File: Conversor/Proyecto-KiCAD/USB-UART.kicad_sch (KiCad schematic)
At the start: 30 parts, among them P11 USB-B, Q5 IRF7425, SW5 Switch, U14 FT232BL, U15 LP2985-3.3, Y1 6 MHz

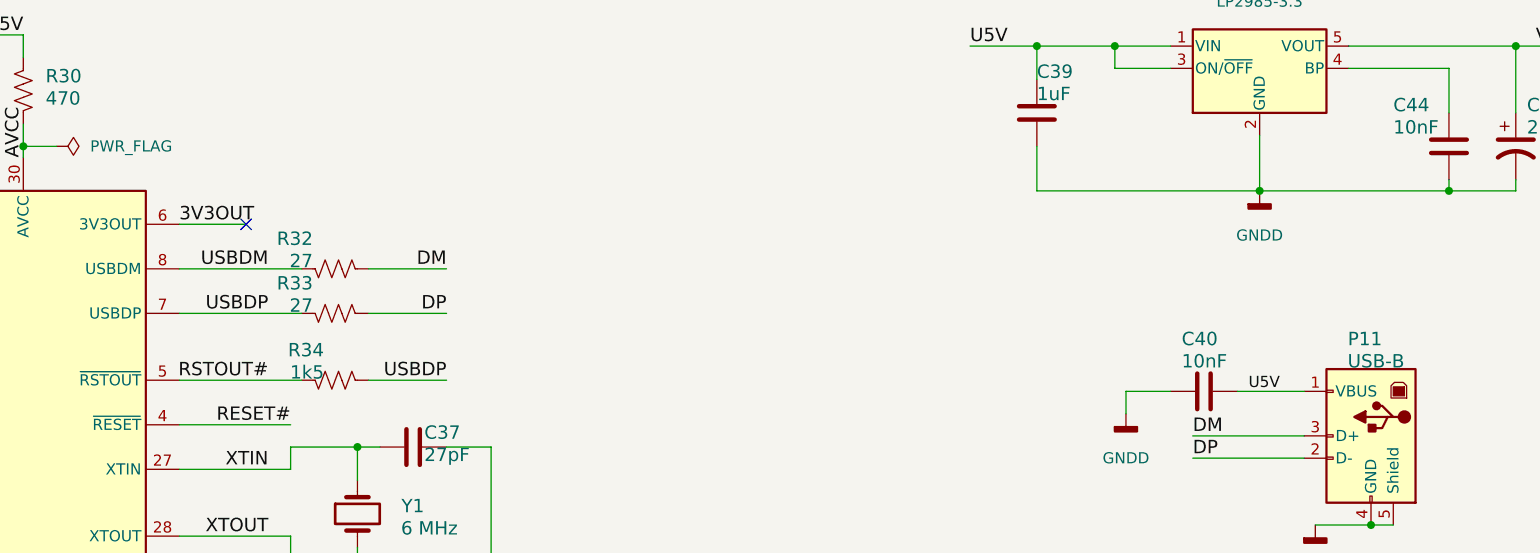
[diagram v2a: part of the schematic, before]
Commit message: Comenzar a asignar footprints a todos los componentes
- Agregado un header para conectar el módulo de tarjeta SD de Arduino
por SPI
- Los GNDs conectados por resistencias nulas son para conectar los GNDs
en caso de que fuera necesario
- Agregar una nota de aplicaión de aislación para I2C (creo que como
estan conectados SDAO y SDAI está bien)
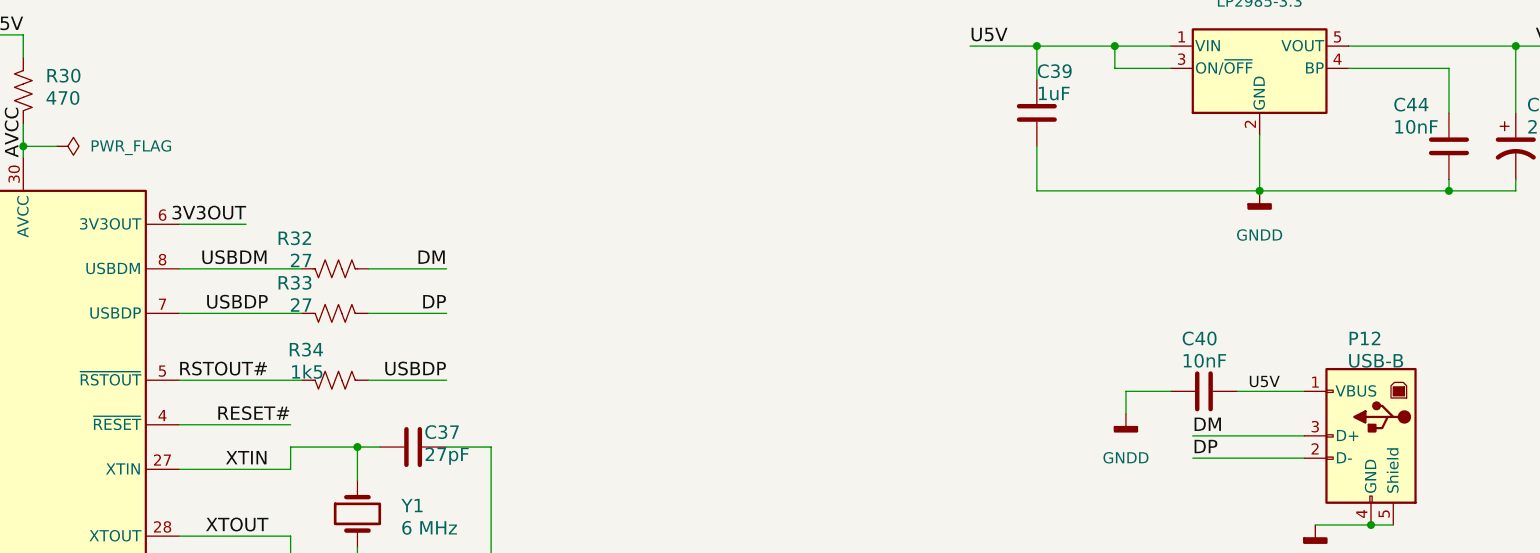
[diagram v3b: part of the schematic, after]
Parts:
- C34, C35, C36, C37, C38, C40, C41, C42, C44, C45, C47: footprint (none) -> Capacitor_SMD:C_1206_3216Metric_Pad1.33x1.80mm_HandSolder
- LED5, LED6: footprint (none) -> Diode_SMD:D_1206_3216Metric_Pad1.42x1.75mm_HandSolder
- P12: renamed from P11; footprint (none) -> Connector_USB:USB_B_Lumberg_2411_02_Horizontal
- R29, R30, R31, R32, R33, R34, R35, R36: footprint (none) -> Resistor_SMD:R_1206_3216Metric_Pad1.30x1.75mm_HandSolder
- Y1: footprint (none) -> Crystal:Crystal_HC18-U_Vertical
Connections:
- no-connect marks 12 -> 11
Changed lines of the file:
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@@
   (no_connect (at 96.52 107.95))
   (no_connect (at 50.8 67.31))
-  (no_connect (at 104.14 62.23))
   (no_connect (at 50.8 72.39))
   (no_connect (at 50.8 69.85))
@@
     (effects (font (size 1.524 1.524)) (justify right bottom))
   )
-  (label "3V3OUT" (at 96.52 62.23 0)
-    (effects (font (size 1.524 1.524)) (justify left bottom))
+  (label "3V3OUT" (at 104.14 62.23 180)
+    (effects (font (size 1.524 1.524)) (justify right bottom))
   )
   (label "U5V" (at 57.15 189.23 90)
@@
       (effects (font (size 1.524 1.524)) (justify right top))
     )
-    (property "Footprint" "" (id 2) (at 127 88.5952 0)
+    (property "Footprint" "Capacitor_SMD:C_1206_3216Metric_Pad1.33x1.80mm_HandSolder" (id 2) (at 127 88.5952 0)
       (effects (font (size 1.27 1.27)) hide)
     )
@@
       (effects (font (size 1.524 1.524)) (justify right top))
     )
-    (property "Footprint" "" (id 2) (at 114.046 66.294 90)
+    (property "Footprint" "Resistor_SMD:R_1206_3216Metric_Pad1.30x1.75mm_HandSolder" (id 2) (at 114.046 66.294 90)
       (effects (font (size 1.27 1.27)) hide)
     )
@@
       (effects (font (size 1.524 1.524)) (justify left bottom))
     )
-    (property "Footprint" "" (id 2) (at 187.96 132.08 0)
+    (property "Footprint" "Diode_SMD:D_1206_3216Metric_Pad1.42x1.75mm_HandSolder" (id 2) (at 187.96 132.08 0)
       (effects (font (size 1.27 1.27)) hide)
     )
@@
       (effects (font (size 1.524 1.524)) (justify left bottom))
     )
-    (property "Footprint" "" (id 2) (at 47.9552 171.45 0)
+    (property "Footprint" "Capacitor_SMD:C_1206_3216Metric_Pad1.33x1.80mm_HandSolder" (id 2) (at 47.9552 171.45 0)
       (effects (font (size 1.27 1.27)) hide)
     )
@@
       (effects (font (size 1.524 1.524)) (justify left bottom))
     )
-    (property "Footprint" "" (id 2) (at 188.976 120.904 90)
+    (property "Footprint" "Resistor_SMD:R_1206_3216Metric_Pad1.30x1.75mm_HandSolder" (id 2) (at 188.976 120.904 90)
       (effects (font (size 1.27 1.27)) hide)
     )
@@
       (effects (font (size 1.524 1.524)) (justify left bottom))
     )
-    (property "Footprint" "" (id 2) (at 204.216 120.904 90)
+    (property "Footprint" "Resistor_SMD:R_1206_3216Metric_Pad1.30x1.75mm_HandSolder" (id 2) (at 204.216 120.904 90)
       (effects (font (size 1.27 1.27)) hide)
     )
@@
   (symbol (lib_id "Connector:USB_B") (at 232.41 86.36 0) (mirror y) (unit 1)
     (in_bom yes) (on_board yes)
-    (property "Reference" "P11" (id 0) (at 233.68 76.2 0)
+    (property "Reference" "P12" (id 0) (at 233.68 76.2 0)
       (effects (font (size 1.524 1.524)) (justify left bottom))
     )
@@
       (effects (font (size 1.524 1.524)) (justify left bottom))
     )
-    (property "Footprint" "" (id 2) (at 228.6 87.63 0)
+    (property "Footprint" "Connector_USB:USB_B_Lumberg_2411_02_Horizontal" (id 2) (at 228.6 87.63 0)
       (effects (font (size 1.27 1.27)) hide)
     )
@@
       (effects (font (size 1.524 1.524)) (justify right top))
     )
-    (property "Footprint" "" (id 2) (at 114.046 78.994 90)
+    (property "Footprint" "Resistor_SMD:R_1206_3216Metric_Pad1.30x1.75mm_HandSolder" (id 2) (at 114.046 78.994 90)
       (effects (font (size 1.27 1.27)) hide)
     )
@@
       (effects (font (size 1.524 1.524)) (justify left bottom))
     )
-    (property "Footprint" "" (id 2) (at 203.2 132.08 0)
+    (property "Footprint" "Diode_SMD:D_1206_3216Metric_Pad1.42x1.75mm_HandSolder" (id 2) (at 203.2 132.08 0)
       (effects (font (size 1.27 1.27)) hide)
     )
@@
       (effects (font (size 1.524 1.524)) (justify left bottom))
     )
-    (property "Footprint" "" (id 2) (at 79.756 46.736 90)
+    (property "Footprint" "Resistor_SMD:R_1206_3216Metric_Pad1.30x1.75mm_HandSolder" (id 2) (at 79.756 46.736 90)
       (effects (font (size 1.27 1.27)) hide)
     )
@@
       (effects (font (size 1.524 1.524)) (justify right top))
     )
-    (property "Footprint" "" (id 2) (at 256.8448 121.92 0)
+    (property "Footprint" "Capacitor_SMD:C_1206_3216Metric_Pad1.33x1.80mm_HandSolder" (id 2) (at 256.8448 121.92 0)
       (effects (font (size 1.27 1.27)) hide)
     )
@@
       (effects (font (size 1.524 1.524)) (justify left bottom))
     )
-    (property "Footprint" "" (id 2) (at 112.014 157.734 90)
+    (property "Footprint" "Resistor_SMD:R_1206_3216Metric_Pad1.30x1.75mm_HandSolder" (id 2) (at 112.014 157.734 90)
       (effects (font (size 1.27 1.27)) hide)
     )
@@
       (effects (font (size 1.524 1.524)) (justify left bottom))
     )
-    (property "Footprint" "" (id 2) (at 116.84 95.25 0)
+    (property "Footprint" "Crystal:Crystal_HC18-U_Vertical" (id 2) (at 116.84 95.25 0)
       (effects (font (size 1.27 1.27)) hide)
     )
@@
       (effects (font (size 1.524 1.524)) (justify left bottom))
     )
-    (property "Footprint" "" (id 2) (at 38.354 172.974 90)
+    (property "Footprint" "Resistor_SMD:R_1206_3216Metric_Pad1.30x1.75mm_HandSolder" (id 2) (at 38.354 172.974 90)
       (effects (font (size 1.27 1.27)) hide)
     )
@@
       (effects (font (size 1.524 1.524)) (justify right top))
     )
-    (property "Footprint" "" (id 2) (at 226.3648 120.65 0)
+    (property "Footprint" "Capacitor_SMD:C_1206_3216Metric_Pad1.33x1.80mm_HandSolder" (id 2) (at 226.3648 120.65 0)
       (effects (font (size 1.27 1.27)) hide)
     )
@@
       (effects (font (size 1.524 1.524)) (justify right top))
     )
-    (property "Footprint" "" (id 2) (at 114.046 71.374 90)
+    (property "Footprint" "Resistor_SMD:R_1206_3216Metric_Pad1.30x1.75mm_HandSolder" (id 2) (at 114.046 71.374 90)
       (effects (font (size 1.27 1.27)) hide)
     )
@@
       (effects (font (size 1.524 1.524)) (justify right top))
     )
-    (property "Footprint" "" (id 2) (at 216.2048 120.65 0)
+    (property "Footprint" "Capacitor_SMD:C_1206_3216Metric_Pad1.33x1.80mm_HandSolder" (id 2) (at 216.2048 120.65 0)
       (effects (font (size 1.27 1.27)) hide)
     )
@@
       (effects (font (size 1.524 1.524)) (justify left bottom))
     )
-    (property "Footprint" "" (id 2) (at 242.2652 57.15 0)
+    (property "Footprint" "Capacitor_SMD:C_1206_3216Metric_Pad1.33x1.80mm_HandSolder" (id 2) (at 242.2652 57.15 0)
       (effects (font (size 1.27 1.27)) hide)
     )
@@
       (effects (font (size 1.524 1.524)) (justify right top))
     )
-    (property "Footprint" "" (id 2) (at 127 103.8352 0)
+    (property "Footprint" "Capacitor_SMD:C_1206_3216Metric_Pad1.33x1.80mm_HandSolder" (id 2) (at 127 103.8352 0)
       (effects (font (size 1.27 1.27)) hide)
     )
@@
       (effects (font (size 1.524 1.524)) (justify left bottom))
     )
-    (property "Footprint" "" (id 2) (at 105.1052 173.99 0)
+    (property "Footprint" "Capacitor_SMD:C_1206_3216Metric_Pad1.33x1.80mm_HandSolder" (id 2) (at 105.1052 173.99 0)
       (effects (font (size 1.27 1.27)) hide)
     )
@@
       (effects (font (size 1.524 1.524)) (justify left bottom))
     )
-    (property "Footprint" "" (id 2) (at 65.7352 162.56 0)
+    (property "Footprint" "Capacitor_SMD:C_1206_3216Metric_Pad1.33x1.80mm_HandSolder" (id 2) (at 65.7352 162.56 0)
       (effects (font (size 1.27 1.27)) hide)
     )
@@
       (effects (font (size 1.524 1.524)) (justify right top))
     )
-    (property "Footprint" "" (id 2) (at 246.6848 121.92 0)
+    (property "Footprint" "Capacitor_SMD:C_1206_3216Metric_Pad1.33x1.80mm_HandSolder" (id 2) (at 246.6848 121.92 0)
       (effects (font (size 1.27 1.27)) hide)
     )
@@
       (effects (font (size 1.524 1.524)) (justify right top))
     )
-    (property "Footprint" "" (id 2) (at 217.17 80.3148 0)
-      (effects (font (size 1.27 1.27)) hide)
-    )
+    (property "Footprint" "Capacitor_SMD:C_1206_3216Metric_Pad1.33x1.80mm_HandSolder" (id 2) (at 217.17 80.3148 0)
+      (effects (font (size 1.27 1.27)) hide)
+    )

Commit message: Comenzar el layout de componentes de la PCB
- Todos los componentes con footprints asignados (preliminar)
- Organizados los componentes de la placa adaptadora en el esquema del
PCB (usando como guia aproximada la placa adaptadora)
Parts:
- C39: footprint (none) -> Capacitor_SMD:C_1206_3216Metric_Pad1.33x1.80mm_HandSolder
- C43, C46: footprint (none) -> Capacitor_THT:CP_Radial_D6.3mm_P2.50mm
- SW5: footprint (none) -> Button_Switch_THT:SW_PUSH_6mm
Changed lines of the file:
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@@
       (effects (font (size 1.524 1.524)) (justify left bottom))
     )
-    (property "Footprint" "" (id 2) (at 195.2752 53.34 0)
+    (property "Footprint" "Capacitor_SMD:C_1206_3216Metric_Pad1.33x1.80mm_HandSolder" (id 2) (at 195.2752 53.34 0)
       (effects (font (size 1.27 1.27)) hide)
     )
@@
       (effects (font (size 1.524 1.524)) (justify left bottom))
     )
-    (property "Footprint" "" (id 2) (at 237.49 124.46 0)
+    (property "Footprint" "Capacitor_THT:CP_Radial_D6.3mm_P2.50mm" (id 2) (at 237.49 124.46 0)
       (effects (font (size 1.27 1.27)) hide)
     )
@@
       (effects (font (size 1.524 1.524)) (justify left bottom))
     )
-    (property "Footprint" "" (id 2) (at 248.92 53.34 0)
+    (property "Footprint" "Capacitor_THT:CP_Radial_D6.3mm_P2.50mm" (id 2) (at 248.92 53.34 0)
       (effects (font (size 1.27 1.27)) hide)
     )
@@
       (effects (font (size 1.524 1.524)) (justify right top))
     )
-    (property "Footprint" "" (id 2) (at 88.9 170.18 0)
-      (effects (font (size 1.27 1.27)) hide)
-    )
+    (property "Footprint" "Button_Switch_THT:SW_PUSH_6mm" (id 2) (at 88.9 170.18 0)
+      (effects (font (size 1.27 1.27)) hide)
+    )

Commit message: Reempezar el ordenado de componentes del PCB
- Intentar copiar mas a la placa adaptadora en la parte del DSP (digital)
  - Algunas cosas (como los headers y la parte de USB) se movieron para hacer entrar mejor las cosas
- Layout bastante completo
- Agregados algunos modelos 3D faltantes
Por hacer:
  - Mover y reorganizar la parte del LM5056, porque tiene una pata que va al secundario, y ahora esta muy lejos del area de GND2
  - Ver como reorganizar un poco para que no queden esquinas vacias
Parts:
- C43: footprint Capacitor_THT:CP_Radial_D6.3mm_P2.50mm -> Capacitor_THT:CP_Radial_D4.0mm_P1.50mm
- C46: footprint Capacitor_THT:CP_Radial_D6.3mm_P2.50mm -> Capacitor_THT:CP_Radial_D4.0mm_P2.00mm
- U14: footprint Package_QFP:LQFP-48_7x7mm_P0.5mm -> Package_DFN_QFN:QFN-32-1EP_7x7mm_P0.65mm_EP5.4x5.4mm
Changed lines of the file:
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@@
       (effects (font (size 1.27 1.27)) (justify left))
     )
-    (property "Footprint" "Package_QFP:LQFP-48_7x7mm_P0.5mm" (id 2) (at 99.06 118.11 0)
+    (property "Footprint" "Package_DFN_QFN:QFN-32-1EP_7x7mm_P0.65mm_EP5.4x5.4mm" (id 2) (at 99.06 118.11 0)
       (effects (font (size 1.27 1.27)) hide)
     )
@@
       (effects (font (size 1.524 1.524)) (justify left bottom))
     )
-    (property "Footprint" "Capacitor_THT:CP_Radial_D6.3mm_P2.50mm" (id 2) (at 237.49 124.46 0)
+    (property "Footprint" "Capacitor_THT:CP_Radial_D4.0mm_P1.50mm" (id 2) (at 237.49 124.46 0)
       (effects (font (size 1.27 1.27)) hide)
     )
@@
       (effects (font (size 1.524 1.524)) (justify left bottom))
     )
-    (property "Footprint" "Capacitor_THT:CP_Radial_D6.3mm_P2.50mm" (id 2) (at 248.92 53.34 0)
+    (property "Footprint" "Capacitor_THT:CP_Radial_D4.0mm_P2.00mm" (id 2) (at 248.92 53.34 0)
       (effects (font (size 1.27 1.27)) hide)
     )

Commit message: Terminar la parte digital de la PCB (incluidas las pistas)
- Hay que ver si la clearance de 0.254mm para el plano de GNDD esta bien
- Cambiar la footprint del FTDI por la version correcta
- Borrar R37, R38 y R39 (usadas para corregir errores del ERC)
Por hacer:
  - Terminar las otras dos partes de la placa
  - Consultar si esta bien lo que hice hasta ahora
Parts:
- U14: footprint Package_DFN_QFN:QFN-32-1EP_7x7mm_P0.65mm_EP5.4x5.4mm -> Package_QFP:LQFP-32_7x7mm_P0.8mm
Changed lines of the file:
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@@
       (effects (font (size 1.27 1.27)) (justify left))
     )
-    (property "Footprint" "Package_DFN_QFN:QFN-32-1EP_7x7mm_P0.65mm_EP5.4x5.4mm" (id 2) (at 99.06 118.11 0)
+    (property "Footprint" "Package_QFP:LQFP-32_7x7mm_P0.8mm" (id 2) (at 99.06 118.11 0)
       (effects (font (size 1.27 1.27)) hide)
     )

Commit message: Continuar el emprolijado de la PCB
- Agregar modelos faltantes y reemplazar incorrectos
- Agregar los constraints de MayerPCB
  - Corregir los errores y warnings de DRC no relacionados con Silkscreen Overlap
Por hacer:
  - Lo mismo del anterior commit
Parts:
- Y1: footprint Crystal:Crystal_HC18-U_Vertical -> Crystal:Resonator-2Pin_W10.0mm_H5.0mm
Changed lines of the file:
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@@
       (effects (font (size 1.524 1.524)) (justify left bottom))
     )
-    (property "Footprint" "Crystal:Crystal_HC18-U_Vertical" (id 2) (at 116.84 95.25 0)
+    (property "Footprint" "Crystal:Resonator-2Pin_W10.0mm_H5.0mm" (id 2) (at 116.84 95.25 0)
       (effects (font (size 1.27 1.27)) hide)
     )
